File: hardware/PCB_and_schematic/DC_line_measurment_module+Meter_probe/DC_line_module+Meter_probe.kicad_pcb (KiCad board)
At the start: 2 copper layers, 100 x 100 mm, 89 parts, among them J1 GND, J2 POWER_RS485, J3 PROBE_CONN, J4 Conn_01x06, J6 IN, J7 OUT, J8 GND, Q1 BC807, Q10 BC807, Q11 BC817, Q12 BC807, Q13 BC807, Q14 BC817, Q15 BC807, Q16 BC807, Q17 BC807, Q18 BC807, Q19 BC807, Q2 BC807, Q20 IRF540N, Q3 BC807, Q4 BC807, Q5 BC807, Q6 BC807, Q7 BC807, Q8 BC807, Q9 BC807, U10 AMS1117-5.0, U12 74HC595, U13 AP74700, U3 74HC595, U4 ST485EBDR, U5 74HC595, U6 ULN2803A, U7 74HC595, U8 ST485EBDR, U9 74HC14

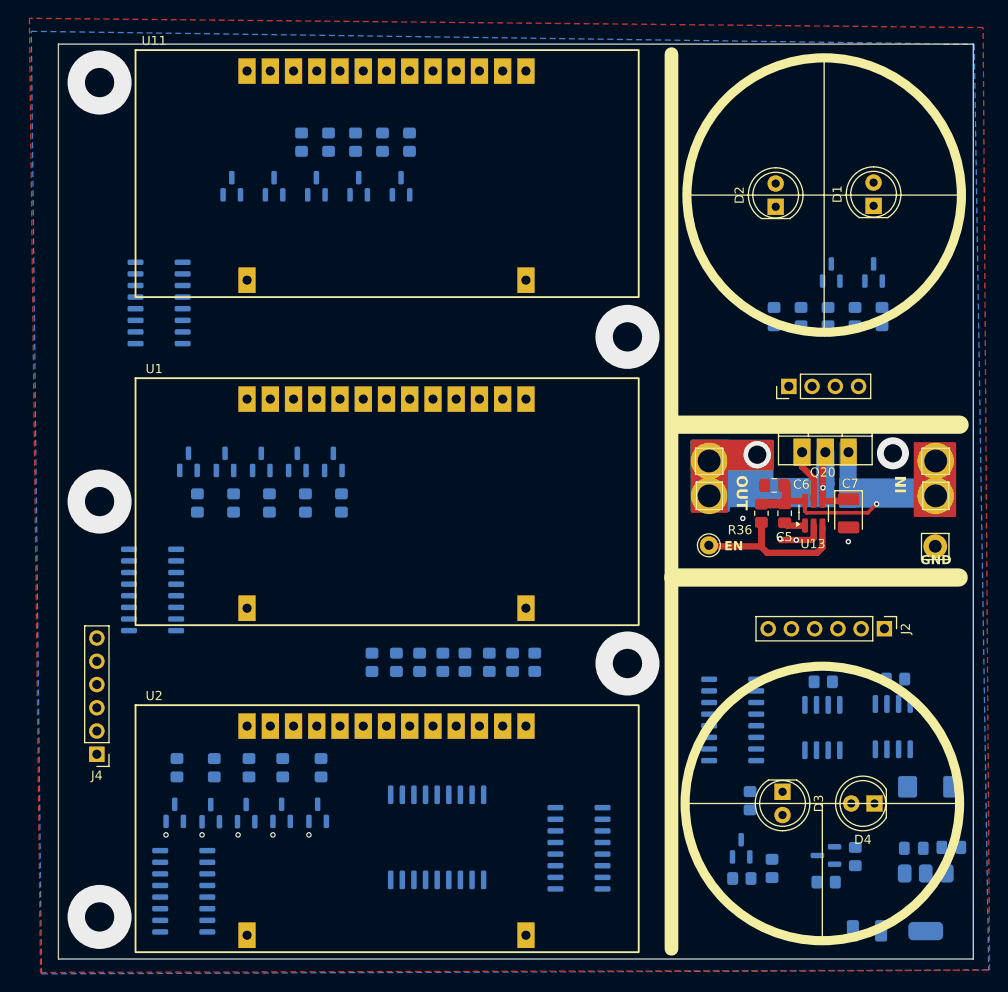
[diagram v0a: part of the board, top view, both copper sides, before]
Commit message: Routing display and probe
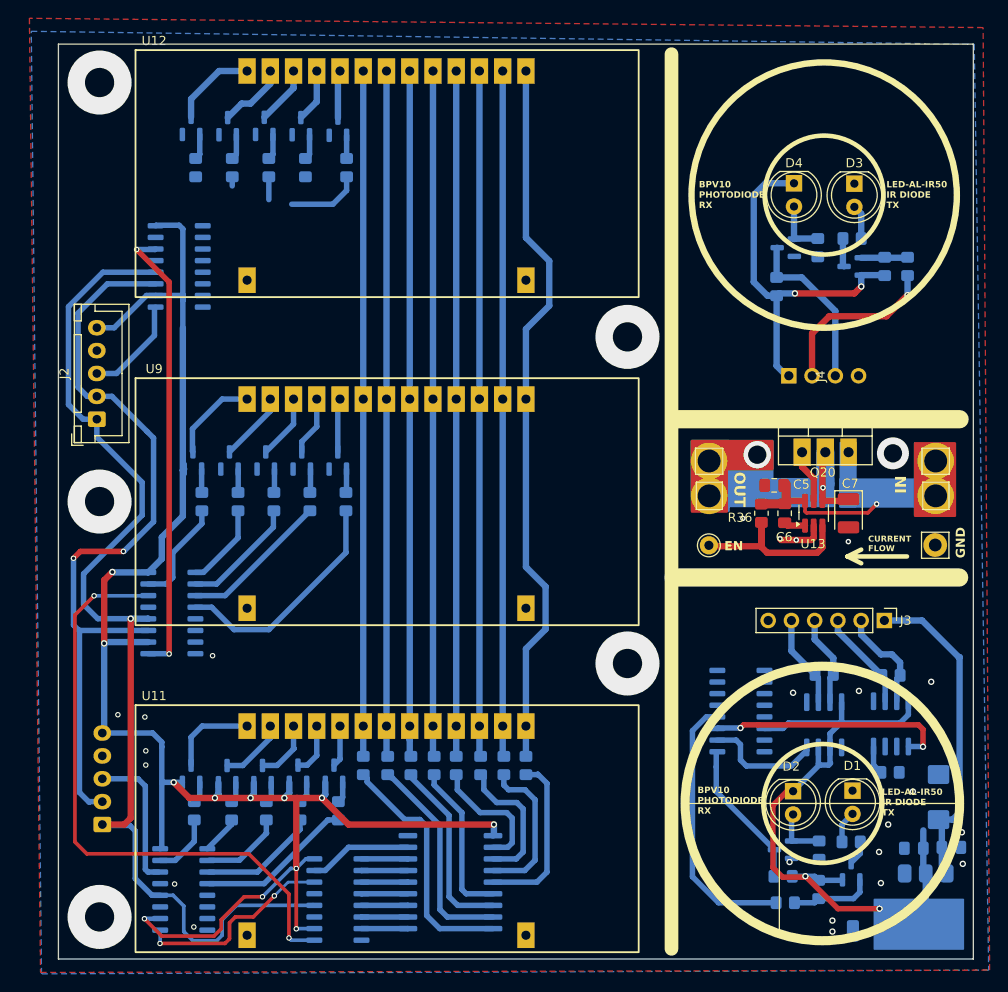
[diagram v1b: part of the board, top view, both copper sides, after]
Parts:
- removed the J4 at (171.2, 107.6)
- added J1: DATA_INPUT, Connector_JST:JST_XH_B5B-XH-A_1x05_P2.50mm_Vertical, B.Cu at (171.8, 115.3)
- added J2: DATA_BRIDGE, Connector_JST:JST_XH_B5B-XH-A_1x05_P2.50mm_Vertical, F.Cu at (171.2, 71.0)
- added R37: 10K, Resistor_SMD:R_0805_2012Metric_Pad1.20x1.40mm_HandSolder, B.Cu at (257.9, 109.6)
- J4: renamed from J3; moved to B.Cu
- R36: value 0R -> 1k
- moved U8 26.9 mm to (197.6, 123.5)
- moved Q7 23.9 mm to (181.5, 38.9)
- moved R10 23.5 mm to (182.0, 43.5), turned to -90 degrees
- moved R9 16.7 mm to (186.0, 43.5), turned to -90 degrees
- moved Q6 15.8 mm to (185.5, 39.0)
- moved R31 15.6 mm to (259.8, 54.3), turned to -90 degrees
- moved Q1 13.3 mm to (197.6, 39.0)
- moved Q3 12.3 mm to (253.7, 120.4)
- moved R3 11.9 mm to (253.7, 117.2), turned to 180 degrees
- moved R17 11.3 mm to (200.3, 108.8)
- moved R18 11.3 mm to (203.0, 108.8)
- moved R21 11.3 mm to (205.5, 108.8)
- moved R22 11.3 mm to (208.1, 108.8)
- moved R25 11.3 mm to (210.5, 108.8)
- moved R27 11.3 mm to (213.2, 108.8)
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- renumbered C3 to C1, C1 to C2, C2 to C3, C6 to C5, C5 to C6, D3 to D1, D4 to D2, D1 to D3, D2 to D4, J2 to J3, J6 to J5, J8 to J6, J1 to J7, J7 to J8, Q19 to Q1, Q1 to Q10, Q7 to Q11, Q13 to Q12, Q2 to Q13, Q8 to Q14, Q14 to Q15, Q3 to Q16, Q9 to Q17, Q5 to Q18, Q10 to Q19, Q18 to Q2, Q12 to Q3, Q11 to Q4, Q17 to Q5, Q16 to Q6, Q15 to Q7, Q4 to Q8, Q6 to Q9, R35 to R1, R31 to R10, R20 to R11, R19 to R12, R4 to R13, R6 to R14, R1 to R15, R7 to R16, R12 to R17, R11 to R18, R21 to R19, R34 to R2, R22 to R20, R13 to R21, R14 to R22, R2 to R23, R8 to R24, R15 to R25, R23 to R26, R16 to R27, R24 to R28, R17 to R29, R28 to R3, R18 to R30, R30 to R31, R3 to R32, R9 to R33, R5 to R34, R10 to R35, R29 to R4, R27 to R5, R33 to R6, R26 to R7, R25 to R8, R32 to R9, U9 to U1, U6 to U10, U2 to U11, U11 to U12, U12 to U2, U4 to U3, U8 to U4, U10 to U5, U5 to U6, U3 to U8, U1 to U9
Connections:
- D4 pad 1: +5V -> +5V_B
- J4 pad 1: +5V -> +5V_B
- J4 pad 2: /METER_RX -> /METER_RX_B
- J4 pad 3: /METER_TX -> /METER_TX_B
- Q12 pad 2: +5V -> +5V_B
- Q15 pad 3: /METER_TX -> /METER_TX_B
- Q4 pad 3: Net-(Q11-C) -> Net-(Q4-C)
- R26 pad 2: +5V -> +5V_B
- R28 pad 1: +5V -> +5V_B
- R28 pad 2: /METER_TX -> /METER_TX_B
- R31 pad 2: /METER_RX -> /METER_RX_B
- R7 pad 2: Net-(Q11-C) -> Net-(Q4-C)
- R8 pad 2: Net-(R25-Pad2) -> Net-(R8-Pad2)
- U1 pad 1: /METER_RX -> Net-(Q4-C)
- U1 pad 2: Net-(R25-Pad2) -> /METER_TX
- U1 pad 3: Net-(Q11-C) -> /METER_RX
- U1 pad 4: /METER_TX -> Net-(R8-Pad2)
- U2 pad 9: Net-(U12-QH') -> SHIFTED_DATA
- U3 pad 4: unconnected-(U4-DI-Pad4) -> Net-(U3-DI)
- U6 pad 14: Net-(U12-QH') -> DATA
- U6 pad 9: SHIFTED_DATA -> Net-(U6-QH')
- U8 pad 14: DATA -> Net-(U6-QH')
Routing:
- net +5V: track 0.00 -> 267.1 mm, vias 0 -> 14
- net LATCH: track 0.00 -> 119.3 mm, vias 0 -> 1
- net CLK: track 0.00 -> 84.4 mm, vias 0 -> 2
- net Net-(U11-A): track 0.00 -> 78.8 mm
- net Net-(U11-E): track 0.00 -> 76.4 mm
- net Net-(U11-F): track 0.00 -> 75.0 mm
- net Net-(U11-D): track 0.00 -> 75.0 mm
- net Net-(U11-C): track 0.00 -> 75.0 mm
- net Net-(U11-B): track 0.00 -> 75.0 mm
- net Net-(U11-Px): track 0.00 -> 74.9 mm
- net Net-(U11-G): track 0.00 -> 74.9 mm
- net Net-(U7-SER): track 0.00 -> 67.1 mm, vias 0 -> 2
- net Net-(U2-SER): track 0.00 -> 50.1 mm, vias 0 -> 2
- net +5V_B: track 0.00 -> 40.6 mm, vias 0 -> 2
- net +12V: track 0.00 -> 35.8 mm
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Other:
- board text added: "+5V RX TX GND"
- board text added: "AP74700 IDEAL DIODE"
- board text added: "BPV10 PHOTODIODE RX"
- board text added: "CURRENT FLOW"
- board text added: "GND TX-A TX-B RX-A RX-B +12V"
- board text added: "LED-AL-IR50 IR DIODE TX"
- board text added: "Reading head for energy meters"

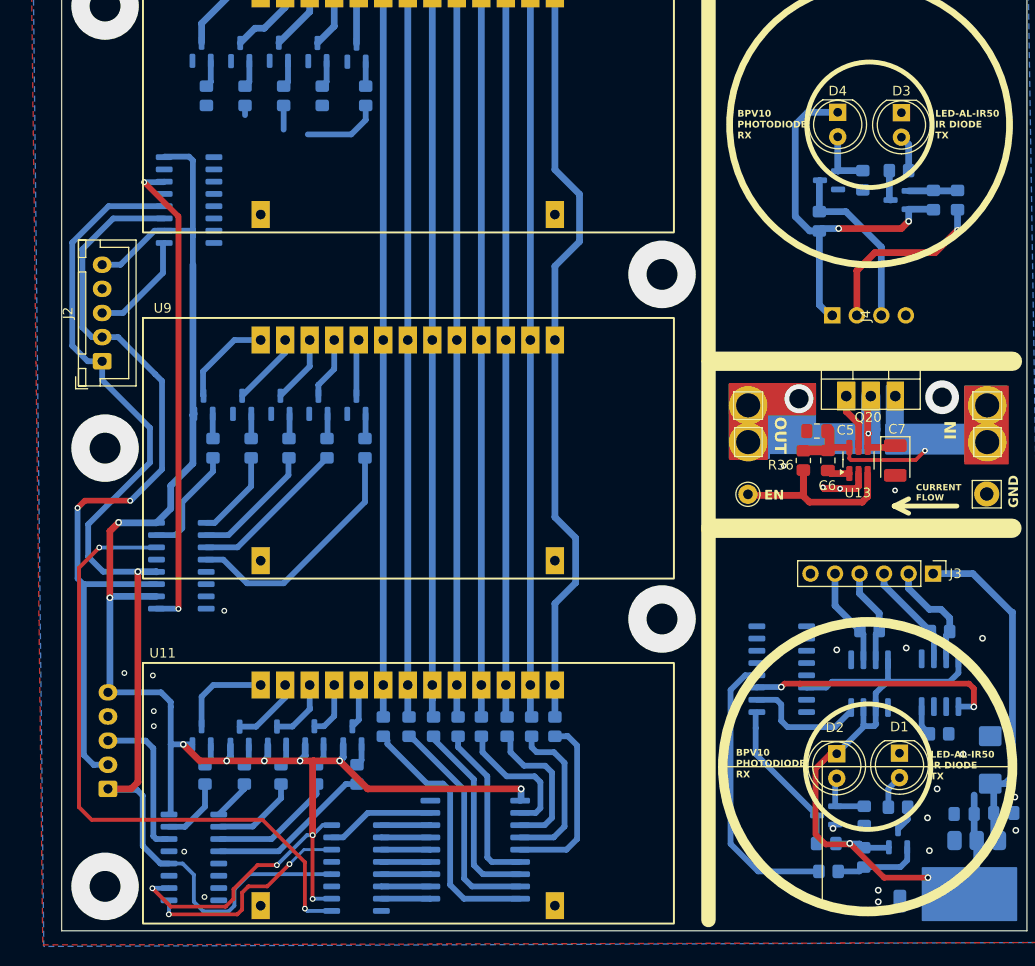
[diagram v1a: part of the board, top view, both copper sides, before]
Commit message: Display pcb routing
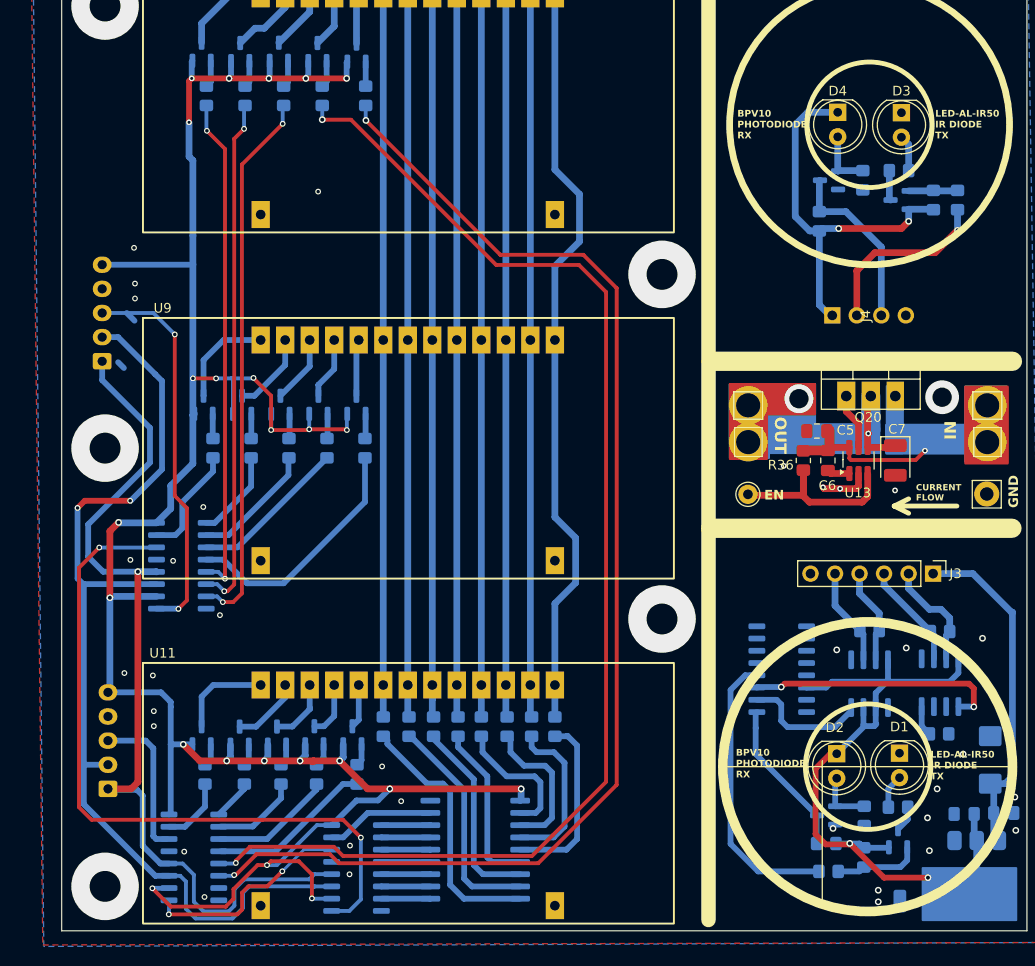
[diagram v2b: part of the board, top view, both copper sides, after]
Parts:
- removed U2: 74HC595, Package_SO:SO-16_3.9x9.9mm_P1.27mm
- J2: moved to B.Cu
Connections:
- R1 pad 2: Net-(U2-QE) -> O5
- R10 pad 2: Net-(U2-QA) -> O3
- R2 pad 2: Net-(U2-QD) -> O4
- R6 pad 2: Net-(U2-QC) -> O6
- R9 pad 2: Net-(U2-QB) -> O2
- U6 pad 5: unconnected-(U6-QF-Pad5) -> O4
- U6 pad 6: unconnected-(U6-QG-Pad6) -> O5
- U7 pad 5: unconnected-(U7-QF-Pad5) -> O3
- U7 pad 6: unconnected-(U7-QG-Pad6) -> O2
- U7 pad 7: unconnected-(U7-QH-Pad7) -> O6
- U7 pad 9: Net-(U2-SER) -> SHIFTED_DATA
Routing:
- net O4: track 0.00 -> 133.6 mm, vias 0 -> 2
- net O5: track 0.00 -> 132.1 mm, vias 0 -> 2
- net O6: track 0.00 -> 56.7 mm, vias 0 -> 2
- net +5V: track 267.1 -> 323.3 mm, vias 14 -> 26
- net O2: track 0.00 -> 53.6 mm, vias 0 -> 2
- net O3: track 0.00 -> 52.1 mm, vias 0 -> 2
- net Net-(U2-SER): track 50.1 -> 0.00 mm, vias 2 -> 0
- net SHIFTED_DATA: track 11.2 -> 41.2 mm, vias 0 -> 2
- net LATCH: track 119.3 -> 94.4 mm
- net CLK: track 84.4 -> 103.2 mm
- net Net-(U2-QE): track 8.12 -> 0.00 mm
- net Net-(U7-SER): track 67.1 -> 74.1 mm
- net Net-(U2-QC): track 2.50 -> 0.00 mm
- net Net-(U2-QB): track 1.00 -> 0.00 mm
- net DISP1_A2: track 7.62 -> 8.37 mm
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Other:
- board text added: "+5V GND DATA CLK LATCH"
- board text added: "Reading head for energy meters via RS485"
- board text added: "SHIFT"

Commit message: Add first concept of tl494 power supply
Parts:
- moved C2 63.2 mm to (202.2, 127.6)
- moved C3 63.2 mm to (198.1, 127.7)
- moved C4 63.2 mm to (193.0, 136.7)
- moved C5 63.2 mm to (182.8, 88.0)
- moved C6 63.2 mm to (184.0, 91.1)
- moved C7 63.2 mm to (191.0, 91.1)
- moved D1 63.2 mm to (191.4, 121.4)
- moved D2 63.2 mm to (184.9, 121.4)
- moved D3 63.2 mm to (191.6, 55.0)
- moved D4 63.2 mm to (185.0, 55.0)
- moved J1 63.2 mm to (109.4, 125.1)
- moved J4 63.2 mm to (184.4, 76.0)
- moved J6 63.2 mm to (200.4, 94.5)
- moved J7 63.2 mm to (175.7, 94.6)
- moved J8 63.2 mm to (175.7, 89.2)
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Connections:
- net /METER_RX renamed /Energy meter probe/METER_RX
- net /METER_RX_B renamed /Energy meter probe/METER_RX_B
- net /METER_TX renamed /Energy meter probe/METER_TX
- net /METER_TX_B renamed /Energy meter probe/METER_TX_B

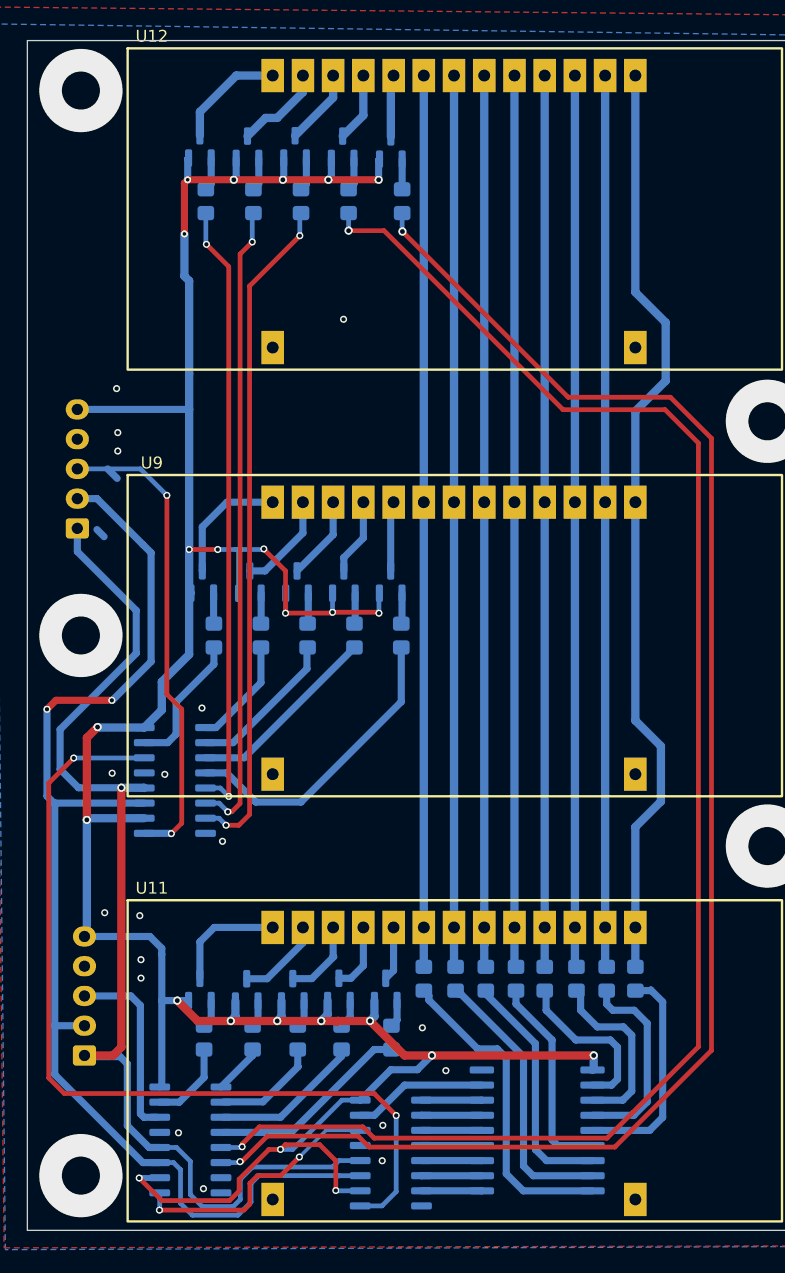
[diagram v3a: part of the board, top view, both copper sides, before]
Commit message: Add aditional 7 segment displays
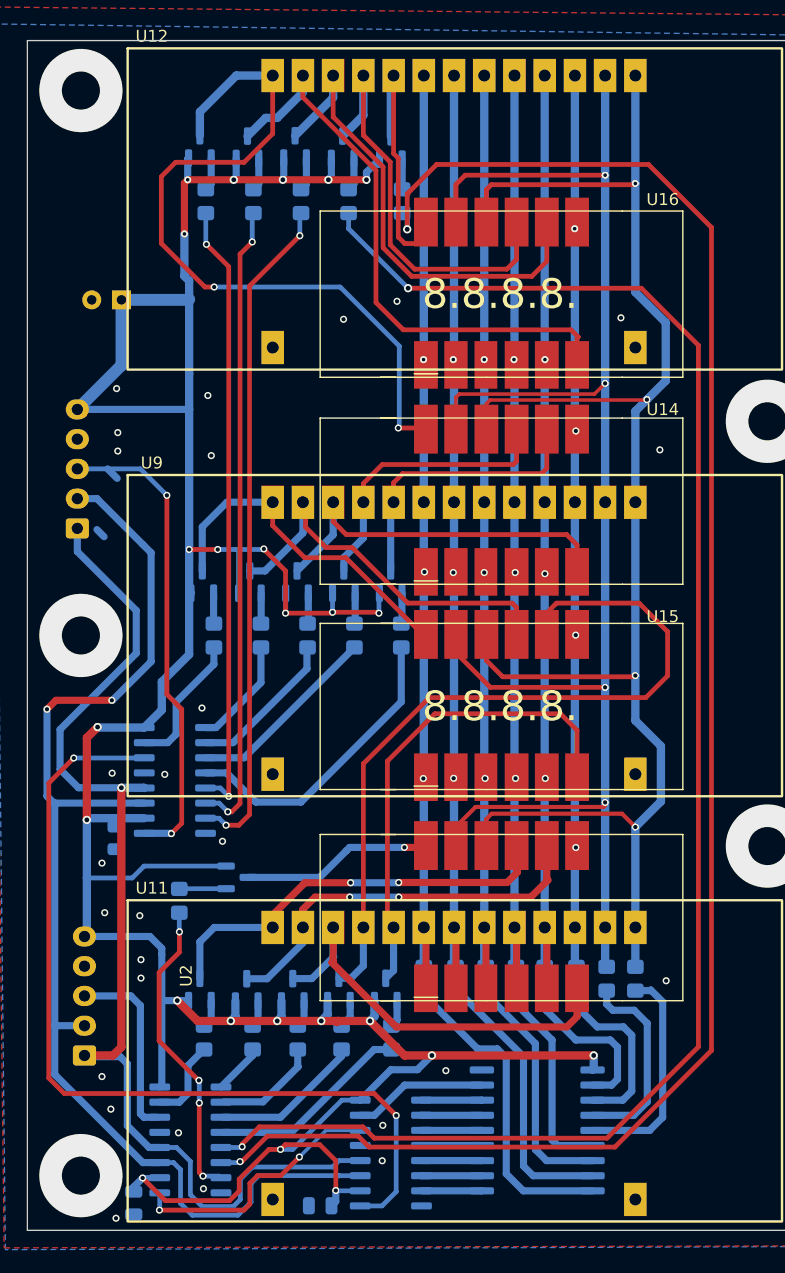
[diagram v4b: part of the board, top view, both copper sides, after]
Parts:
- added C10: C, Capacitor_SMD:C_0805_2012Metric, B.Cu at (112.1, 106.8)
- added C11: C_Polarized, Capacitor_THT:CP_Radial_D10.0mm_P2.50mm, B.Cu at (112.5, 61.6)
- added C8: C, Capacitor_SMD:C_0805_2012Metric, B.Cu at (113.5, 137.5)
- added C9: C, Capacitor_SMD:C_0805_2012Metric, B.Cu at (129.2, 137.7)
- added Q21: BC807, Package_TO_SOT_SMD:SOT-23, B.Cu at (122.2, 110.1)
- added R38: 10k, Resistor_SMD:R_0805_2012Metric_Pad1.20x1.40mm_HandSolder, B.Cu at (117.4, 112.1)
- added U14: CA56-12SURKWA, My-Footprints:4-digit-7-segment-display_smd, F.Cu at (138.1, 82.9)
- added U15: CA56-12SURKWA, My-Footprints:4-digit-7-segment-display_smd, F.Cu at (138.1, 100.2)
- added U16: CA56-12SURKWA, My-Footprints:4-digit-7-segment-display_smd, F.Cu at (138.1, 65.5)
- added U2: CA56-12SURKWA, My-Footprints:4-digit-7-segment-display_smd, F.Cu at (138.1, 117.9)
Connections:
- net Net-(U11-A) renamed DISP_A
- net Net-(U11-B) renamed DISP_B
- net Net-(U11-C) renamed DISP_C
- net Net-(U11-D) renamed DISP_D
- net Net-(U11-E) renamed DISP_E
- net Net-(U11-F) renamed DISP_F
- net Net-(U11-G) renamed DISP_G
- net Net-(U11-Px) renamed DISP_DP
- U6 pad 7: unconnected-(U6-QH-Pad7) -> Net-(U6-QH)
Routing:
- net DISP_B: track 75.0 -> 137.6 mm, vias 0 -> 4
- net DISP_A: track 78.8 -> 141.3 mm, vias 0 -> 4
- net DISP2_A4: track 5.71 -> 65.1 mm
- net DISP3_A1: track 9.39 -> 63.6 mm, vias 0 -> 2
- net DISP3_A2: track 7.59 -> 49.8 mm
- net DISP2_A5: track 4.55 -> 40.8 mm
- net DISP3_A3: track 6.39 -> 41.2 mm
- net +5V: track 323.3 -> 353.9 mm
- net DISP3_A4: track 5.81 -> 35.9 mm
- net DISP2_A3: track 6.69 -> 35.3 mm
- net DISP2_A2: track 7.27 -> 33.3 mm, vias 0 -> 2
- net Net-(U6-QH): track 0.00 -> 26.0 mm, vias 0 -> 4
- net DISP1_A2: track 8.37 -> 33.9 mm
- net DISP2_A1: track 9.68 -> 35.1 mm, vias 0 -> 2
- net DISP1_A3: track 7.03 -> 32.2 mm
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
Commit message: Chceck and update DC module and meter probe pcb
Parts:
- C10, C8, C9: value C -> 100n
- C11: value C_Polarized -> 470u/6,3V
- R17, R18, R21, R22, R25, R27, R29, R30: value 240R -> 200R
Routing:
- net Net-(J8-Pin_1): track 29.4 -> 65.0 mm
- net +5V_B: track 40.6 -> 59.2 mm, vias 2 -> 3
- net Net-(R8-Pad2): track 29.6 -> 45.5 mm
- net /Energy meter probe/METER_TX_B: track 18.5 -> 26.2 mm
- net GND: vias 44 -> 54

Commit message: Bidirectional DC - change shunt resistor
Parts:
- J1, J2: footprint Connector_JST:JST_XH_B5B-XH-A_1x05_P2.50mm_Vertical -> My-Footprints-connectors:JST_XH_B5B-XH-A_1x05_P2.54mm_Vertical
- J3: footprint Connector_PinHeader_2.54mm:PinHeader_1x06_P2.54mm_Vertical -> My-Footprints-connectors:Pin_Header_Straight_1x06_Pitch2.54mm
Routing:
- net LATCH: track 94.4 -> 93.6 mm
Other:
- board text added: "7-SEGMENT DISPLAY 10.2024 V1.0 kwiecinski.github.io"
- board text added: "74HC14"
- board text added: "OPRICAL READING HEAD FOR ENERGY METERS 10.2024 V1.0 kwiecinski.github.io"
- board text added: "OPTICAL READING HEAD FOR ENERGY METERS VIA RS485 10.2024 V1.0 kwiecinski.github.io"
- board text added: "ST485"
- board text removed: "Reading head for energy meters"
- board text removed: "Reading head for energy meters via RS485"

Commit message: add production files
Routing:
- net Net-(J8-Pin_1): track 65.0 -> 38.2 mm
- net +5V_B: track 59.2 -> 40.6 mm, vias 3 -> 2
- net Net-(R8-Pad2): track 45.5 -> 29.6 mm
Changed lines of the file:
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@@
-	)
-	(segment
-		(start 172.75 108.25)
-		(end 176.25 108.25)
-		(width 0.4)
-		(layer "B.Cu")
-		(net 26)
-	)
-	(segment
-		(start 171.75 107.25)
-		(end 172.75 108.25)
-		(width 0.4)
-		(layer "B.Cu")
-		(net 26)
-	)
-	(segment
-		(start 172.0875 89.1625)
-		(end 171.75 89.5)
-		(width 0.4)
-		(layer "B.Cu")
-		(net 26)
 	)
 	(segment
@@
 	)
 	(segment
-		(start 175.725 89.1625)
-		(end 172.0875 89.1625)
-		(width 0.4)
-		(layer "B.Cu")
-		(net 26)
-	)
-	(segment
-		(start 171.75 89.5)
-		(end 171.75 107.25)
-		(width 0.4)
-		(layer "B.Cu")
-		(net 26)
-	)
-	(segment
 		(start 189.5 76)
 		(end 189.5 82)
@@
 		(end 175.415 113.3225)
 		(width 0.6)
-		(layer "B.Cu")
-		(net 40)
-	)
-	(segment
-		(start 173.9 130.5)
-		(end 158 130.5)
-		(width 0.4)
 		(layer "B.Cu")
 		(net 40)
@@
 	)
 	(segment
-		(start 171.5 60.75)
-		(end 162 60.75)
-		(width 0.4)
-		(layer "F.Cu")
-		(net 96)
-	)
-	(segment
 		(start 192.35 66.2875)
 		(end 191.6 67.0375)
 		(width 0.7)
 		(layer "F.Cu")
-		(net 96)
-	)
-	(via
-		(at 171.5 60.75)
-		(size 0.6)
-		(drill 0.3)
-		(layers "F.Cu" "B.Cu")
 		(net 96)
 	)
@@
 		(layer "B.Cu")
 		(net 96)
-	)
-	(segment
-		(start 180.6 60.75)
-		(end 171.5 60.75)
-		(width 0.4)
-		(layer "B.Cu")
-		(net 96)
